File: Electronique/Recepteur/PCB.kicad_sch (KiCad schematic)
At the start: 13 parts, among them J1 USB_A, SW3 SW_Push, SW4 SW_Push, U3 ESP32-S3-MINI-1, U4 TLV75533PDBV

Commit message: edit schema
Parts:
- removed D5: LED, LED_SMD:LED_0603_1608Metric, symbol Device:LED
- removed R2: 470, Resistor_SMD:R_0805_2012Metric, symbol Device:R
- added C3: 100nF, Capacitor_SMD:C_0603_1608Metric_Pad1.08x0.95mm_HandSolder, symbol Device:C
- added C4: 1nF, Capacitor_SMD:C_0603_1608Metric_Pad1.08x0.95mm_HandSolder, symbol Device:C
- C1, C2: value 1µ -> 10µ
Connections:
- net +3.3V: now also C3.2
- net EN (Reset): now also C4.1
- net GND: now also C3.1, C4.2
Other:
- moved on the sheet: U3

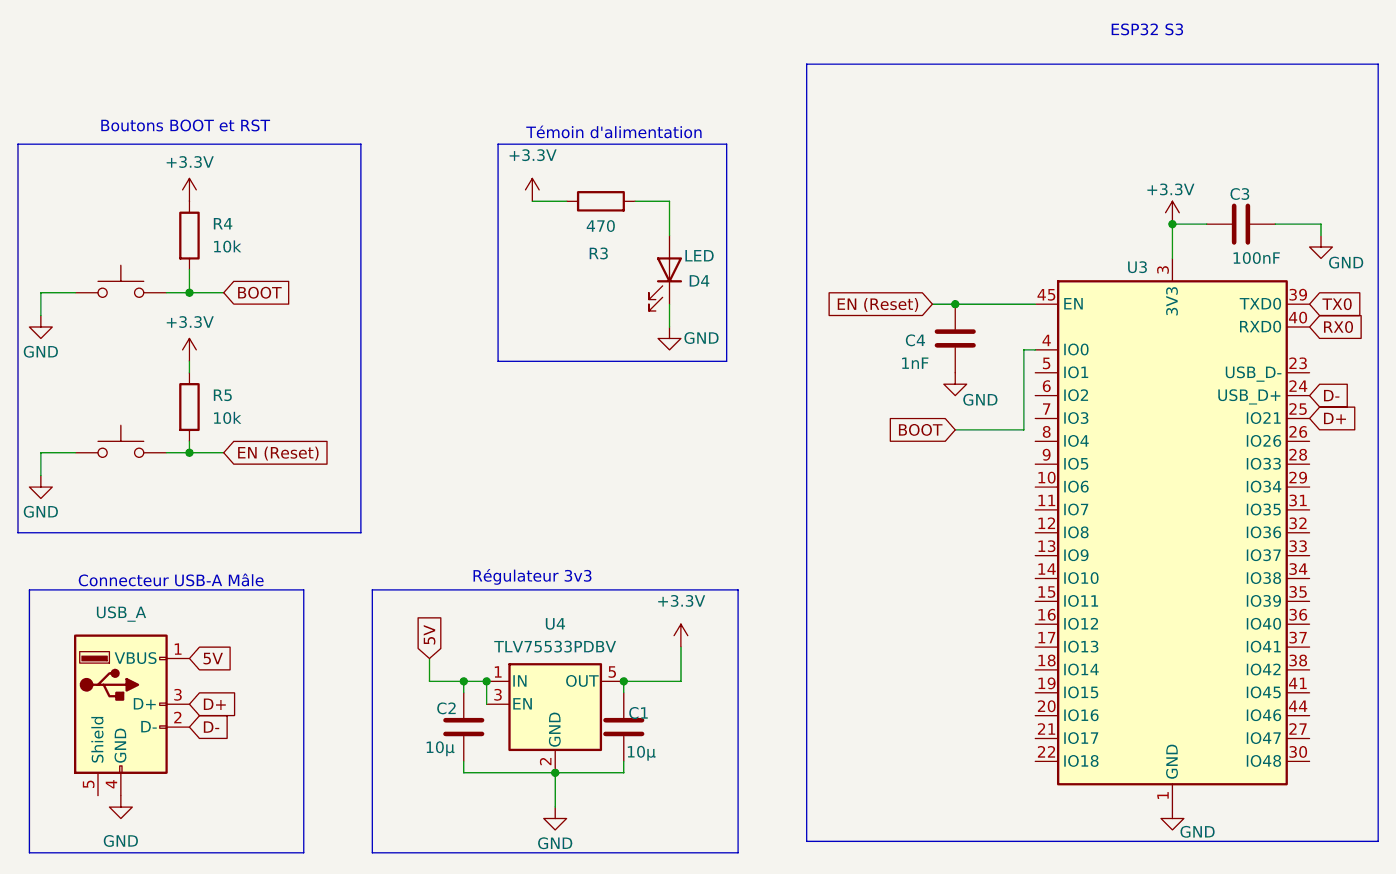
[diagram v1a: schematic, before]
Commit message: update keyboard schematic
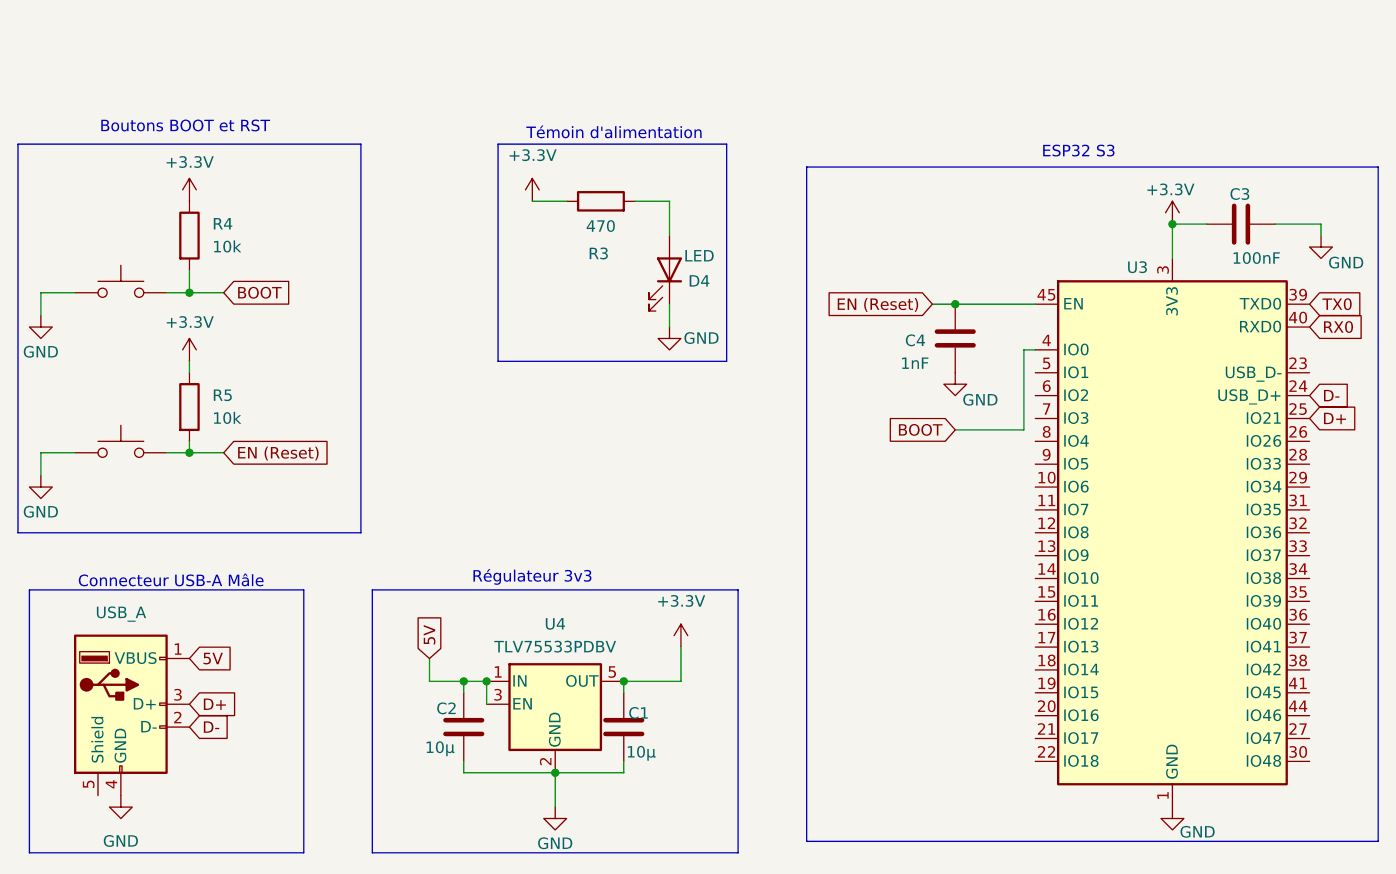
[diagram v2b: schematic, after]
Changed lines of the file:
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@@
 	)
 	(rectangle
-		(start 177.8 25.4)
+		(start 177.8 36.83)
 		(end 241.3 111.76)
 		(stroke
@@
 	(text "ESP32 S3\n\n"
 		(exclude_from_sim no)
-		(at 215.646 22.86 0)
+		(at 208.026 36.322 0)
 		(effects
 			(font
